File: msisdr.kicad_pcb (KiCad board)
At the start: 2 copper layers, 46.3 x 90.7 mm, 84 parts, among them J1 VCC_GPIO, J10 SMA_VHF1, J11 USB_OTG, J12 Conn_01x02, J2 GPIO0, J3 GPIO1, J4 GPIO2, J5 GPIO3, J6 SMA_0_30MHZ, J7 SMA_30_60MHZ, J8 SMA_VHF2, J9 SMA_UHF, U1 msi2500, U2 msi001, U3 RT9193-28, U4 AP7313-30SAG, Y1 24MHz, Y2 24MHZ

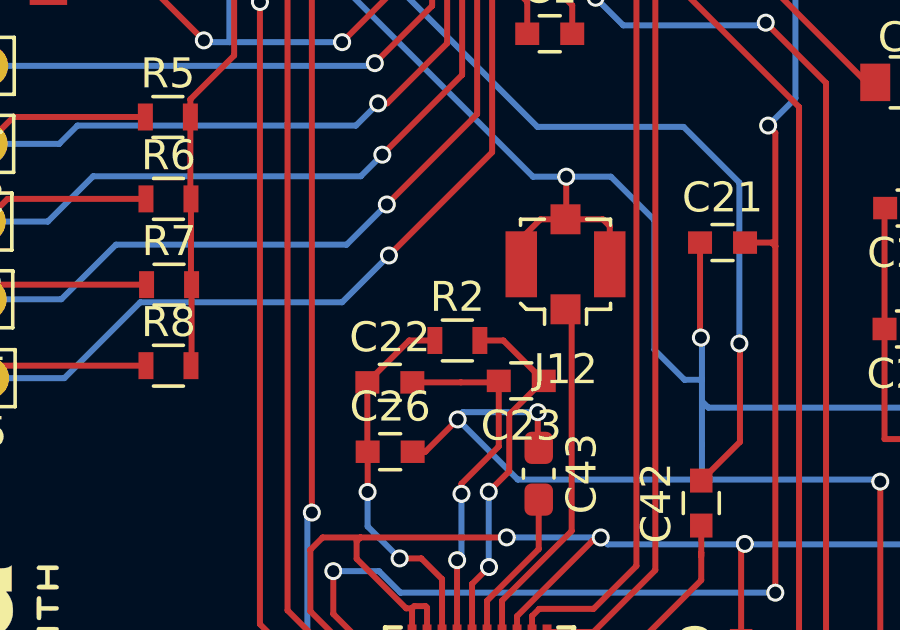
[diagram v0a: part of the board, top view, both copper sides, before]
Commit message: Fixed clearance issue
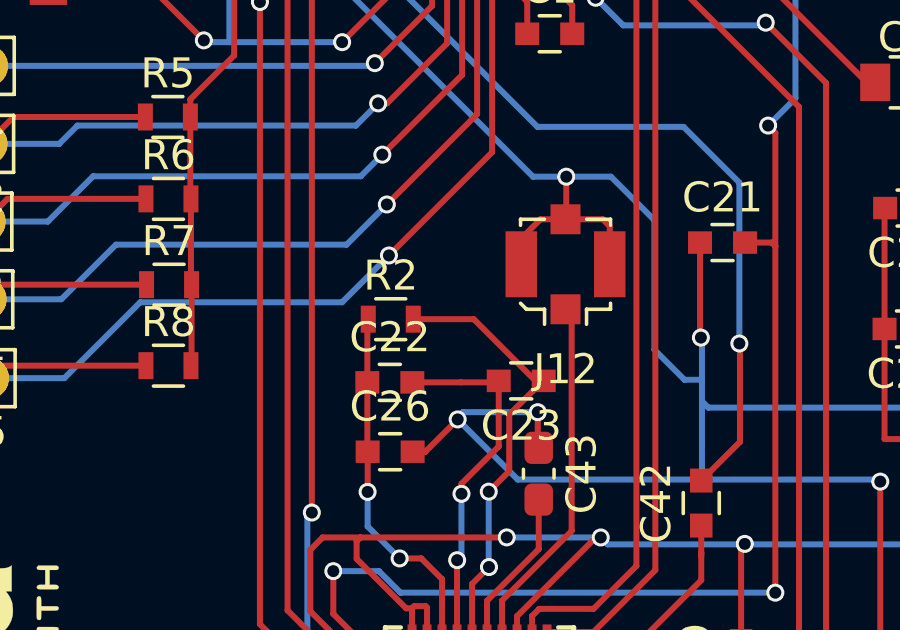
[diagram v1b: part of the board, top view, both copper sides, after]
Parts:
- moved R2 2.33 mm to (132.4, 92.0)
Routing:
- net Net-(C23-Pad1): track 12.1 -> 14.6 mm
- net Net-(C22-Pad1): track 12.6 -> 11.9 mm
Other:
- rule pad_to_mask_clearance: 0.2 -> 0
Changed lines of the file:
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@@
     (thickness 1.6)
     (drawings 7)
-    (tracks 974)
+    (tracks 975)
     (zones 0)
     (modules 84)
@@
     (pad_size 4.064 4.064)
     (pad_drill 3)
-    (pad_to_mask_clearance 0.2)
+    (pad_to_mask_clearance 0)
     (aux_axis_origin 0 0)
     (visible_elements 7FFEFFFF)
@@
       (drillshape 0)
       (scaleselection 1)
-      (outputdirectory "gerberv2/"))
+      (outputdirectory "gerberv3/"))
   )
   (net 0 "")
@@
   )
   (module Resistors_SMD:R_0603 (layer F.Cu)
-    (at 134.62 92.71)
+    (at 132.4 92)
     (descr "Resistor SMD 0603, reflow soldering, Vishay (see dcrcw.pdf)")
     (tags "resistor 0603")
@@
   (segment (start 131.619 94.106) (end 131.619 96.40768) (width 0.2) (layer F.Cu) (net 14))
   (segment (start 131.619 96.40768) (end 131.62972 96.4184) (width 0.2) (layer F.Cu) (net 14))
-  (segment (start 133.015 92.71) (end 131.619 94.106) (width 0.2) (layer F.Cu) (net 14))
-  (segment (start 133.87 92.71) (end 133.015 92.71) (width 0.2) (layer F.Cu) (net 14))
+  (segment (start 131.619 92.031) (end 131.65 92) (width 0.2) (layer F.Cu) (net 14))
+  (segment (start 131.619 94.106) (end 131.619 92.031) (width 0.2) (layer F.Cu) (net 14))
   (segment (start 132.97 57.22) (end 132.97 55.64) (width 0.2) (layer F.Cu) (net 15))
   (segment (start 133.93 54.68) (end 136.019 54.68) (width 0.2) (layer F.Cu) (net 15))
@@
   (segment (start 136.34901 95.18099) (end 136.34901 97.06683) (width 0.2) (layer F.Cu) (net 44))
   (segment (start 137.499 94.056) (end 137.474 94.056) (width 0.2) (layer F.Cu) (net 44))
-  (segment (start 136.153 92.71) (end 137.499 94.056) (width 0.2) (layer F.Cu) (net 44))
-  (segment (start 135.37 92.71) (end 136.153 92.71) (width 0.2) (layer F.Cu) (net 44))
+  (segment (start 137.224002 94.056) (end 137.499 94.056) (width 0.2) (layer F.Cu) (net 44))
+  (segment (start 135.168002 92) (end 137.224002 94.056) (width 0.2) (layer F.Cu) (net 44))
+  (segment (start 133.15 92) (end 135.168002 92) (width 0.2) (layer F.Cu) (net 44))
   (segment (start 131.22148 125.82582) (end 135.16102 125.82582) (width 0.2) (layer F.Cu) (net 45))
   (segment (start 135.16102 125.82582) (end 135.38454 125.6023) (width 0.2) (layer F.Cu) (net 45))

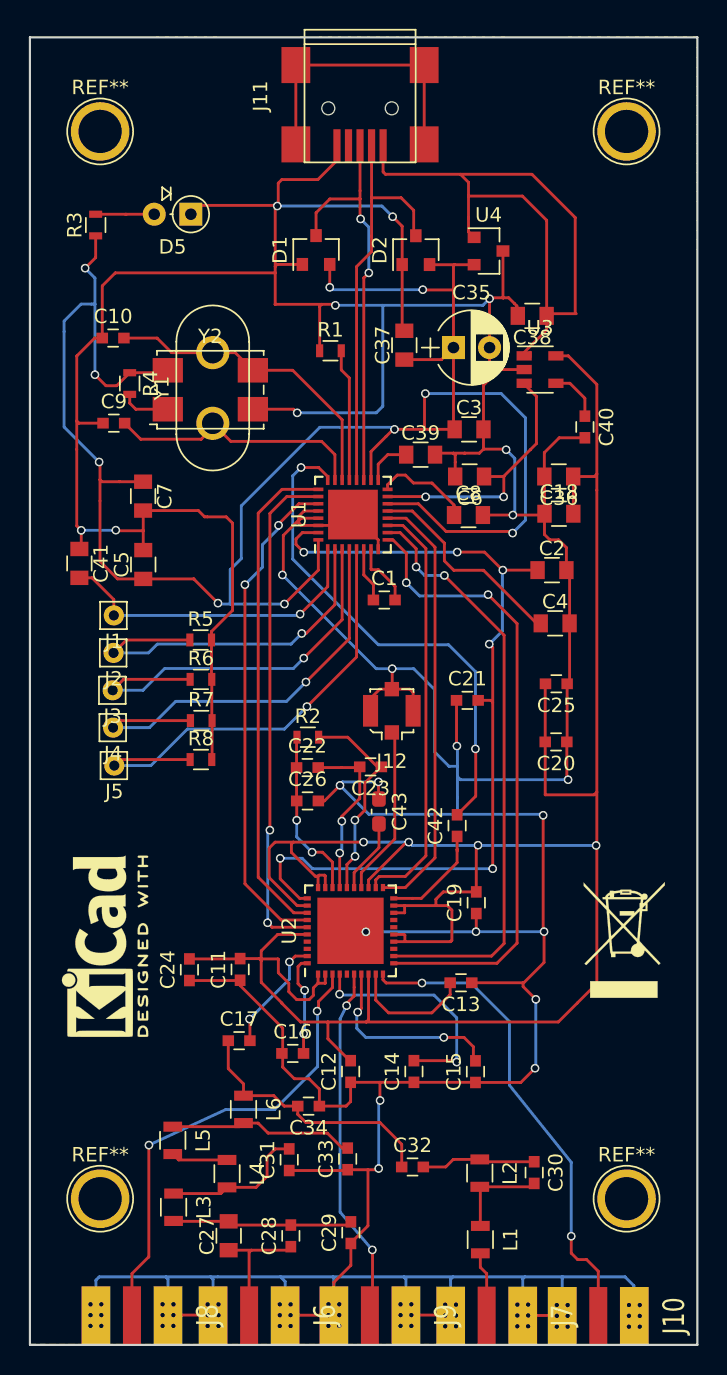
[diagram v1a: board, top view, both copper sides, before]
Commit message: Changed the package of R, C and L to 1206 for hand soldering.
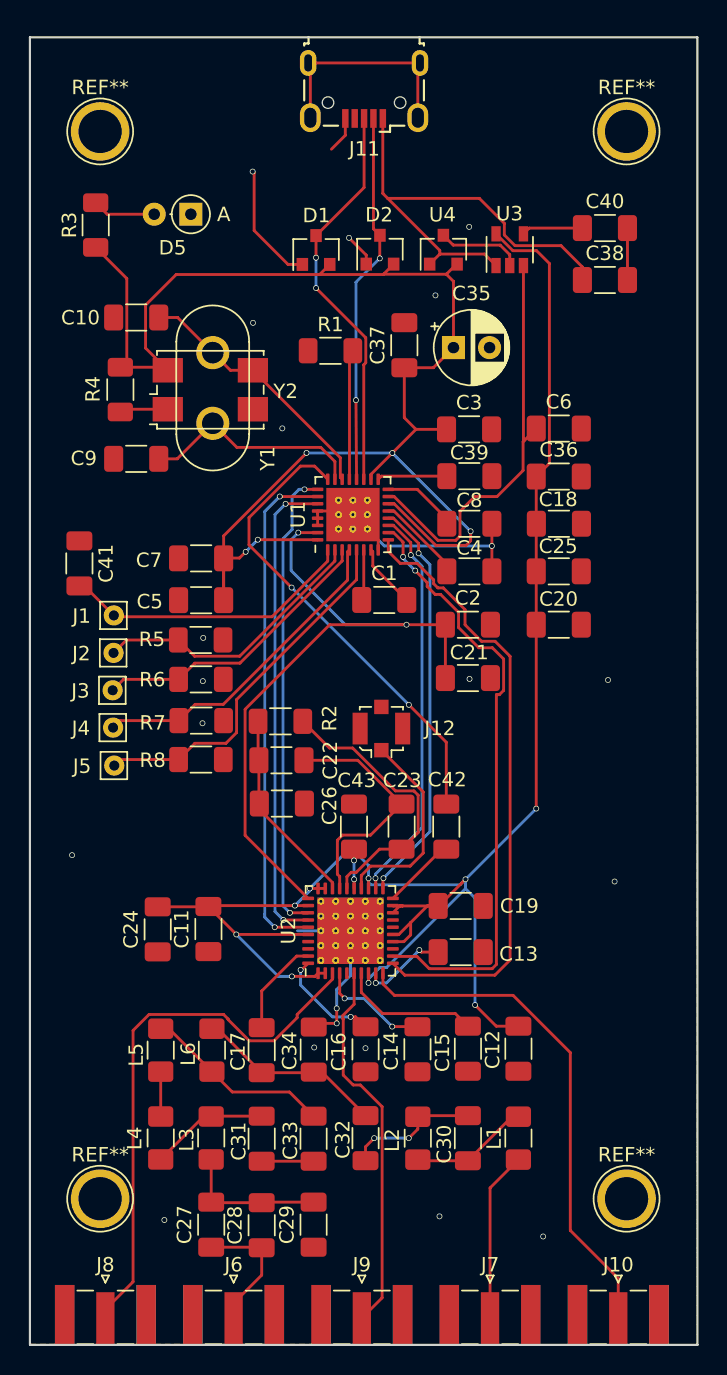
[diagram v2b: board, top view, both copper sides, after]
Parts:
- removed REF***: KiCad-Logo2_6mm_SilkScreen, Symbols:KiCad-Logo2_6mm_SilkScreen
- removed REF***: WEEE-Logo_5.6x8mm_SilkScreen, Symbols:WEEE-Logo_5.6x8mm_SilkScreen
- C1, C10, C11, C12, C13, C14, C15, C16, C17, C19, C20, C21, C22, C23, C24, C25, C26, C28, C29, C30, C31, C32, C33, C34, C40, C42, C9: footprint Capacitors_SMD:C_0603 -> Capacitor_SMD:C_1206_3216Metric_Pad1.33x1.80mm_HandSolder
- C18, C2, C27, C3, C36, C37, C38, C39, C4, C41, C5, C6, C7, C8: footprint Capacitors_SMD:C_0805 -> Capacitor_SMD:C_1206_3216Metric_Pad1.33x1.80mm_HandSolder
- C35: footprint Capacitors_THT:CP_Radial_D5.0mm_P2.50mm -> Capacitor_THT:CP_Radial_D5.0mm_P2.50mm
- C43: footprint Capacitor_SMD:C_0603_1608Metric_Pad1.08x0.95mm_HandSolder -> Capacitor_SMD:C_1206_3216Metric_Pad1.33x1.80mm_HandSolder
- D1, D2, U4: footprint TO_SOT_Packages_SMD:SOT-23 -> Package_TO_SOT_SMD:SOT-23
- D5: footprint Diodes_THT:D_DO-35_SOD27_P2.54mm_Vertical_AnodeUp -> Diode_THT:D_DO-35_SOD27_P2.54mm_Vertical_AnodeUp
- J1, J2, J3, J4, J5: footprint Connectors:Pin_d0.7mm_L6.5mm_W1.8mm_FlatFork -> Connector_Pin:Pin_D0.7mm_L6.5mm_W1.8mm_FlatFork
- J10, J8, J9: footprint sma:SMA_OPL_EMPTYHEAD -> Connector_Coaxial:SMA_Samtec_SMA-J-P-X-ST-EM1_EdgeMount
- J11: footprint Connectors:USB_Mini-B -> Connector_USB:USB_Micro-B_Wuerth_629105150521
- J6, J7: footprint sma:SMA_OPL_EM -> Connector_Coaxial:SMA_Samtec_SMA-J-P-X-ST-EM1_EdgeMount
- L1, L2, L3, L4, L5, L6: footprint Inductors_SMD:L_0805 -> Inductor_SMD:L_1206_3216Metric_Pad1.42x1.75mm_HandSolder
- R1, R2, R3, R4, R5, R6, R7, R8: footprint Resistors_SMD:R_0603 -> Resistor_SMD:R_1206_3216Metric_Pad1.30x1.75mm_HandSolder
- U1: footprint Housings_DFN_QFN:QFN-32-1EP_5x5mm_Pitch0.5mm -> Package_DFN_QFN:QFN-32-1EP_5x5mm_P0.5mm_EP3.7x3.7mm_ThermalVias
- U2: footprint Housings_DFN_QFN:QFN-40-1EP_6x6mm_Pitch0.5mm -> Package_DFN_QFN:QFN-40-1EP_6x6mm_P0.5mm_EP4.6x4.6mm_ThermalVias
- U3: footprint TO_SOT_Packages_SMD:SOT-23-5 -> Package_TO_SOT_SMD:SOT-23-5
- Y1: footprint Crystals:Crystal_HC50_Vertical -> Crystal:Crystal_HC50_Vertical
- Y2: footprint Crystals:Crystal_SMD_7050-4pin_7.0x5.0mm -> Crystal:Crystal_SMD_7050-4Pin_7.0x5.0mm
- moved C40 13.9 mm to (153.0, 56.7), turned to 0 degrees
- moved C12 11.7 mm to (147.0, 113.6)
- moved U3 8.57 mm to (146.4, 58.2), turned to 90 degrees
- moved C20 8.13 mm to (149.8, 84.2)
- moved C25 7.80 mm to (149.8, 80.5)
- moved L1 7.51 mm to (147.0, 119.8)
- moved C6 7.02 mm to (149.8, 70.6), turned to 0 degrees
- moved C4 6.96 mm to (143.6, 80.5)
- moved C2 6.95 mm to (143.5, 84.2)
- moved L5 6.31 mm to (122.2, 113.7)
- moved C7 5.90 mm to (125.0, 79.6), turned to 180 degrees
- moved C38 5.62 mm to (153.0, 60.3), turned to 0 degrees
- moved L3 5.47 mm to (125.7, 119.8)
- moved L4 5.22 mm to (122.2, 119.8)
- moved C30 5.18 mm to (143.5, 119.8)
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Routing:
- net GND: track 476.6 -> 57.1 mm, vias 23 -> 21
- net VRF: track 170.9 -> 128.0 mm, vias 4 -> 9
- net VDIG: track 143.9 -> 107.2 mm, vias 10 -> 5
- net Net-(C38-Pad1): track 46.4 -> 33.1 mm
- net VDDI: track 61.0 -> 48.7 mm, vias 6 -> 2
- net V18-SYNTH: track 18.8 -> 29.0 mm, vias 2 -> 0
- net Net-(C14-Pad2): track 16.3 -> 7.75 mm
- net Net-(C4-Pad1): track 14.6 -> 6.09 mm
- net Net-(J3-Pad1): track 28.5 -> 20.4 mm, vias 1 -> 0
- net Net-(J4-Pad1): track 30.7 -> 22.6 mm, vias 1 -> 0
- net Net-(J7-Pad1): track 4.49 -> 11.8 mm
- net Net-(J5-Pad1): track 32.8 -> 25.5 mm, vias 1 -> 0
- net Net-(J2-Pad1): track 26.3 -> 19.7 mm, vias 1 -> 0
- net VHF_120_250MHZ: track 32.6 -> 38.1 mm, vias 2 -> 0
- net HFPORT: track 18.5 -> 13.3 mm
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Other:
- outline, holes or cut-outs redrawn
